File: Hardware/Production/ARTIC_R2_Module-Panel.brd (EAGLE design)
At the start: 154.2 x 147.3 mm, 2306 parts, among them J101 U.FL, J126 U.FL, J151 U.FL, J176 U.FL, J201 U.FL, J226 U.FL, J25 U.FL, J251 U.FL, J26 U.FL, J276 U.FL, J301 U.FL, J326 U.FL, J351 U.FL, J376 U.FL, J401 U.FL, J426 U.FL, J451 U.FL, J476 U.FL, J51 U.FL, J76 U.FL, K1 TLP3475R, K10 TLP3475R, K11 TLP3475R, K12 TLP3475R, K13 TLP3475R, K14 TLP3475R, K15 TLP3475R, K16 TLP3475R, K17 TLP3475R, K18 TLP3475R, K19 TLP3475R, K2 TLP3475R, K20 TLP3475R, K3 TLP3475R, K4 TLP3475R, K5 TLP3475R, K6 TLP3475R, K7 TLP3475R, K8 TLP3475R, K9 TLP3475R, Q1 5.8A/30V/35mΩ, Q10 5.8A/30V/35mΩ, Q11 5.8A/30V/35mΩ, Q12 5.8A/30V/35mΩ, Q13 5.8A/30V/35mΩ, Q14 5.8A/30V/35mΩ, Q15 5.8A/30V/35mΩ, Q16 5.8A/30V/35mΩ, Q17 5.8A/30V/35mΩ, Q18 5.8A/30V/35mΩ, Q19 5.8A/30V/35mΩ, Q2 5.8A/30V/35mΩ, Q20 5.8A/30V/35mΩ, Q3 5.8A/30V/35mΩ, Q4 5.8A/30V/35mΩ, Q5 5.8A/30V/35mΩ, Q6 5.8A/30V/35mΩ, Q7 5.8A/30V/35mΩ, Q8 5.8A/30V/35mΩ, Q9 5.8A/30V/35mΩ, U1 ADM4210-1, U10 1.8V/100mA, U100 1.8V/100mA, U101 3.0V, U102 ADM4210-1, U103 ARTIC_R2, U104 RFPA0133, U105 AS179-92LF, U106 1.8V/100mA, U107 3.0V, U108 ADM4210-1, U109 ARTIC_R2, U11 3.0V, U110 RFPA0133, U111 AS179-92LF, U112 1.8V/100mA, U113 3.0V, U114 ADM4210-1, U115 ARTIC_R2, U116 RFPA0133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

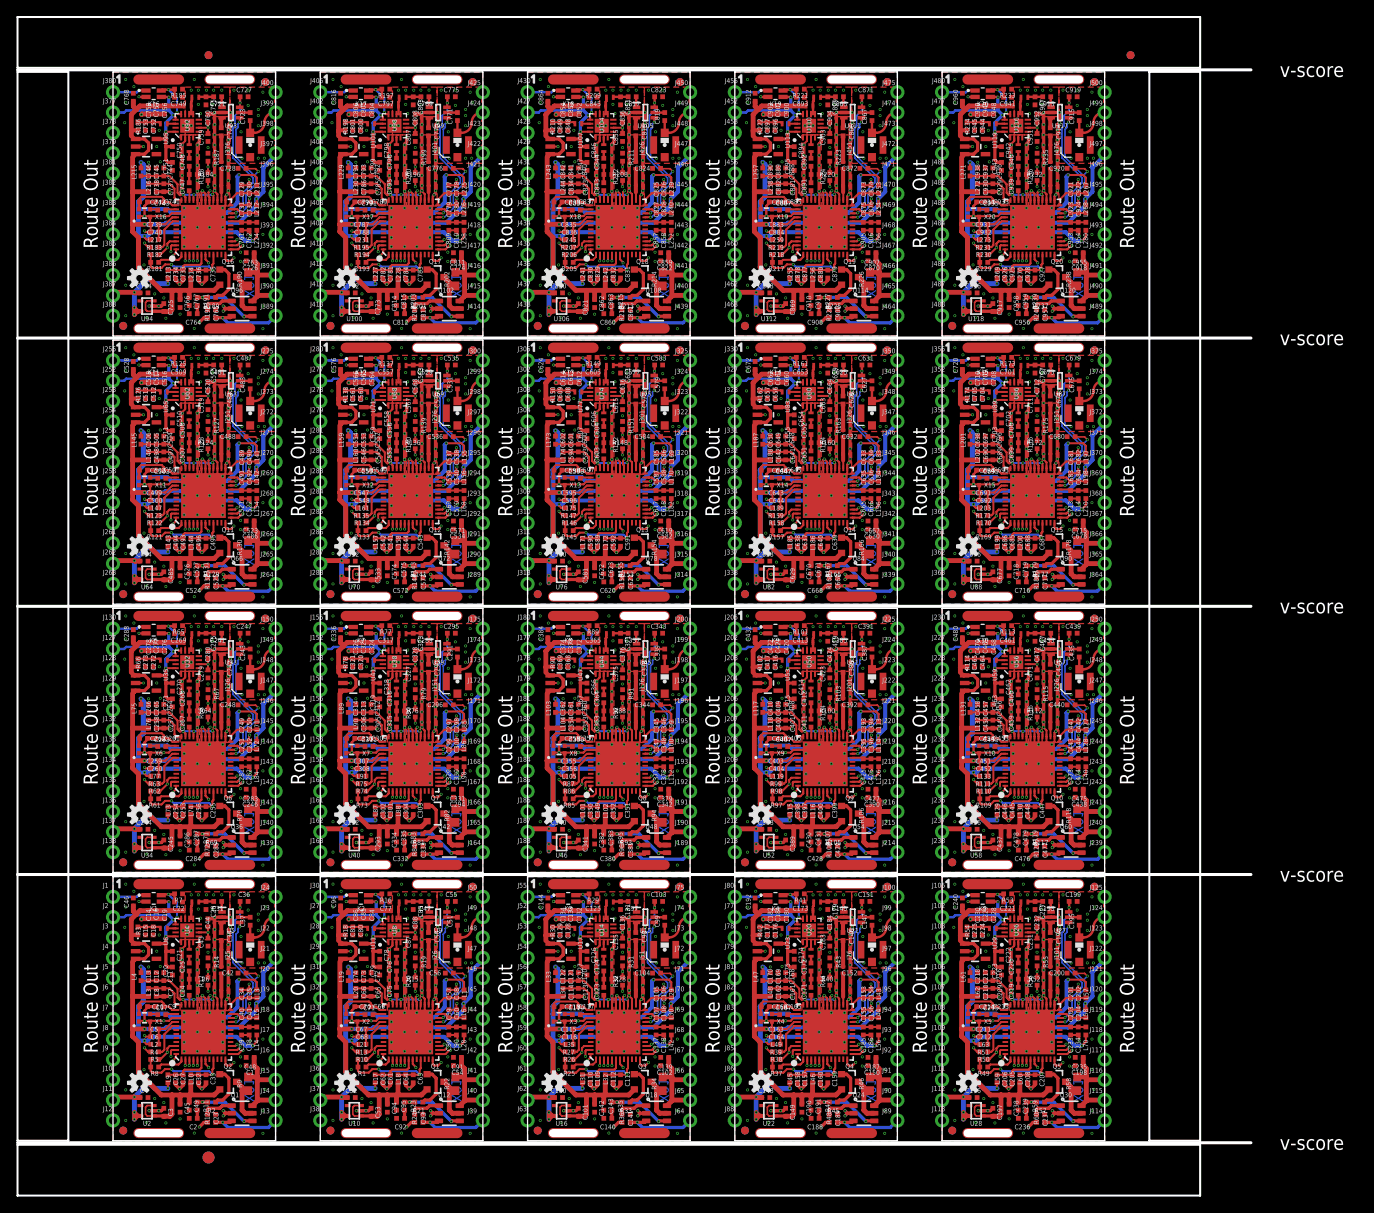
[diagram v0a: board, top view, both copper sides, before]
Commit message: Adding better castellated pads. Correcting cutouts for screen tabs.
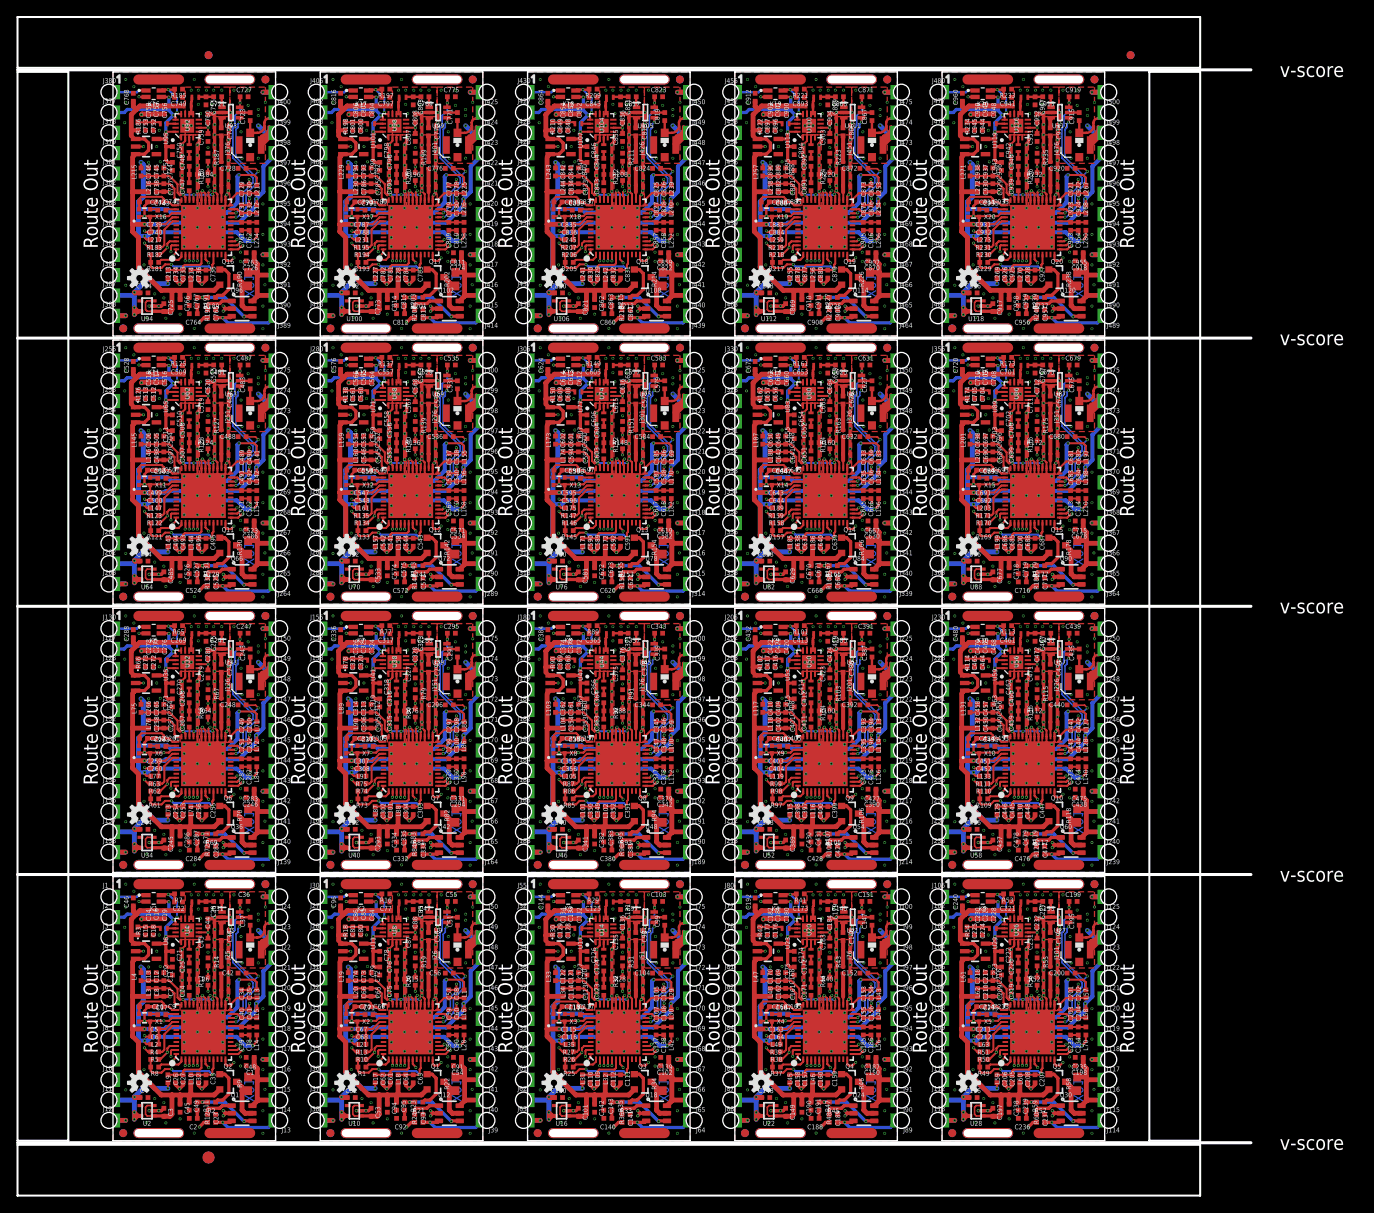
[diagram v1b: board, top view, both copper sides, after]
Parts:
- added LOGO21, LOGO22, LOGO23, LOGO24, LOGO25, LOGO26, LOGO27, LOGO28, LOGO29, LOGO30, LOGO31, LOGO32, LOGO33, LOGO34, LOGO35, LOGO36, LOGO37, LOGO38, LOGO39, LOGO40: OSHW-LOGOS, SparkFun-Aesthetics:OSHW-LOGO-S
- added SPARKX1, SPARKX10, SPARKX11, SPARKX12, SPARKX13, SPARKX14, SPARKX15, SPARKX16, SPARKX17, SPARKX18, SPARKX19, SPARKX2, SPARKX20, SPARKX3, SPARKX4, SPARKX5, SPARKX6, SPARKX7, SPARKX8, SPARKX9: SPARKX-LOGO4, SparkX:SPARKX-MEDIUM
- added U$100, U$126, U$152, U$178, U$204, U$22, U$230, U$256, U$282, U$308, U$334, U$360, U$386, U$412, U$438, U$464, U$48, U$490, U$516, U$74: (no value), output:#SCLK#0
- added U$101, U$127, U$153, U$179, U$205, U$23, U$231, U$257, U$283, U$309, U$335, U$361, U$387, U$413, U$439, U$465, U$49, U$491, U$517, U$75: (no value), output:#COPI#0
- added U$102, U$128, U$154, U$180, U$206, U$232, U$24, U$258, U$284, U$310, U$336, U$362, U$388, U$414, U$440, U$466, U$492, U$50, U$518, U$76: (no value), output:#CIPO#0
- added U$103, U$129, U$155, U$181, U$207, U$233, U$25, U$259, U$285, U$311, U$337, U$363, U$389, U$415, U$441, U$467, U$493, U$51, U$519, U$77: (no value), output:#1#8V_OUT#0
- added U$104, U$130, U$156, U$182, U$208, U$234, U$26, U$260, U$286, U$312, U$338, U$364, U$390, U$416, U$442, U$468, U$494, U$52, U$520, U$78: (no value), output:ARTIC_R20
- added U$105, U$131, U$157, U$183, U$209, U$235, U$261, U$27, U$287, U$313, U$339, U$365, U$391, U$417, U$443, U$469, U$495, U$53, U$79: (no value), output:10
- added U$106, U$107, U$108, U$109, U$132, U$133, U$134, U$135, U$158, U$159, U$160, U$161, U$184, U$185, U$186, U$187, U$210, U$211, U$212, U$213, U$236, U$237, U$238, U$239, U$262, U$263, U$264, U$265, U$28, U$288, U$289, U$29, U$290, U$291, U$30, U$31, U$314, U$315, U$316, U$317, U$340, U$341, U$342, U$343, U$366, U$367, U$368, U$369, U$392, U$393, U$394, U$395, U$418, U$419, U$420, U$421, U$444, U$445, U$446, U$447, U$470, U$471, U$472, U$473, U$496, U$497, U$498, U$499, U$54, U$55, U$56, U$57, U$80, U$81, U$82, U$83: (no value), output:#GND#0
- added U$110, U$136, U$162, U$188, U$214, U$240, U$266, U$292, U$318, U$32, U$344, U$370, U$396, U$422, U$448, U$474, U$500, U$58, U$84: (no value), output:#PWR_EN#0
- added U$111, U$112, U$137, U$138, U$163, U$164, U$189, U$190, U$215, U$216, U$241, U$242, U$267, U$268, U$293, U$294, U$319, U$320, U$33, U$34, U$345, U$346, U$371, U$372, U$397, U$398, U$423, U$424, U$449, U$450, U$475, U$476, U$501, U$502, U$59, U$60, U$85, U$86: (no value), output:#VIN#0
- added U$113, U$139, U$165, U$191, U$217, U$243, U$269, U$295, U$321, U$347, U$35, U$373, U$399, U$425, U$451, U$477, U$503, U$61, U$87: (no value), output:#FLSH_SCLK#0
- added U$114, U$140, U$166, U$192, U$218, U$244, U$270, U$296, U$322, U$348, U$36, U$374, U$400, U$426, U$452, U$478, U$504, U$62, U$88: (no value), output:#FLSH_SI#0
- added U$115, U$141, U$167, U$193, U$219, U$245, U$271, U$297, U$323, U$349, U$37, U$375, U$401, U$427, U$453, U$479, U$505, U$63, U$89: (no value), output:#FLSH_CEN#0
- added U$116, U$142, U$168, U$194, U$220, U$246, U$272, U$298, U$324, U$350, U$376, U$38, U$402, U$428, U$454, U$480, U$506, U$64, U$90: (no value), output:#FLSH_SO#0
- added U$117, U$143, U$169, U$195, U$221, U$247, U$273, U$299, U$325, U$351, U$377, U$39, U$403, U$429, U$455, U$481, U$507, U$65, U$91: (no value), output:#3#3V_OUT#0
- added U$118, U$144, U$170, U$196, U$222, U$248, U$274, U$300, U$326, U$352, U$378, U$40, U$404, U$430, U$456, U$482, U$508, U$66, U$92: (no value), output:#ANTENNA#0
- added U$119, U$145, U$171, U$197, U$223, U$249, U$275, U$301, U$327, U$353, U$379, U$405, U$41, U$431, U$457, U$483, U$509, U$67, U$93: (no value), output:#G8#0
- added U$120, U$146, U$172, U$198, U$224, U$250, U$276, U$302, U$328, U$354, U$380, U$406, U$42, U$432, U$458, U$484, U$510, U$68, U$94: (no value), output:#3#0V_OUT#0
- added U$121, U$147, U$173, U$199, U$225, U$251, U$277, U$303, U$329, U$355, U$381, U$407, U$43, U$433, U$459, U$485, U$511, U$69, U$95: (no value), output:#BOOT#0
- added U$122, U$148, U$174, U$200, U$226, U$252, U$278, U$304, U$330, U$356, U$382, U$408, U$434, U$44, U$460, U$486, U$512, U$70, U$96: (no value), output:#INT1#0
- added U$123, U$149, U$175, U$201, U$227, U$253, U$279, U$305, U$331, U$357, U$383, U$409, U$435, U$45, U$461, U$487, U$513, U$71, U$97: (no value), output:#INT2#0
- added U$124, U$150, U$176, U$202, U$228, U$254, U$280, U$306, U$332, U$358, U$384, U$410, U$436, U$46, U$462, U$488, U$514, U$72, U$98: (no value), output:#RESETB#0
- added U$125, U$151, U$177, U$203, U$21, U$229, U$255, U$281, U$307, U$333, U$359, U$385, U$411, U$437, U$463, U$47, U$489, U$515, U$73, U$99: (no value), output:#CS#0
- J1, J10, J100, J102, J103, J104, J105, J106, J107, J108, J109, J11, J110, J111, J112, J113, J114, J115, J116, J117, J118, J119, J12, J120, J121, J122, J123, J124, J125, J127, J128, J129, J13, J130, J131, J132, J133, J134, J135, J136, J137, J138, J139, J14, J140, J141, J142, J143, J144, J145, J146, J147, J148, J149, J15, J150, J152, J153, J154, J155, J156, J157, J158, J159, J16, J160, J161, J162, J163, J164, J165, J166, J167, J168, J169, J17, J170, J171, J172, J173, J174, J175, J177, J178, J179, J18, J180, J181, J182, J183, J184, J185, J186, J187, J188, J189, J19, J190, J191, J192, J193, J194, J195, J196, J197, J198, J199, J2, J20, J200, J202, J203, J204, J205, J206, J207, J208, J209, J21, J210, J211, J212, J213, J214, J215, J216, J217, J218, J219, J22, J220, J221, J222, J223, J224, J225, J227, J228, J229, J23, J230, J231, J232, J233, J234, J235, J236, J237, J238, J239, J24, J240, J241, J242, J243, J244, J245, J246, J247, J248, J249, J250, J252, J253, J254, J255, J256, J257, J258, J259, J260, J261, J262, J263, J264, J265, J266, J267, J268, J269, J27, J270, J271, J272, J273, J274, J275, J277, J278, J279, J28, J280, J281, J282, J283, J284, J285, J286, J287, J288, J289, J29, J290, J291, J292, J293, J294, J295, J296, J297, J298, J299, J3, J30, J300, J302, J303, J304, J305, J306, J307, J308, J309, J31, J310, J311, J312, J313, J314, J315, J316, J317, J318, J319, J32, J320, J321, J322, J323, J324, J325, J327, J328, J329, J33, J330, J331, J332, J333, J334, J335, J336, J337, J338, J339, J34, J340, J341, J342, J343, J344, J345, J346, J347, J348, J349, J35, J350, J352, J353, J354, J355, J356, J357, J358, J359, J36, J360, J361, J362, J363, J364, J365, J366, J367, J368, J369, J37, J370, J371, J372, J373, J374, J375, J377, J378, J379, J38, J380, J381, J382, J383, J384, J385, J386, J387, J388, J389, J39, J390, J391, J392, J393, J394, J395, J396, J397, J398, J399, J4, J40, J400, J402, J403, J404, J405, J406, J407, J408, J409, J41, J410, J411, J412, J413, J414, J415, J416, J417, J418, J419, J42, J420, J421, J422, J423, J424, J425, J427, J428, J429, J43, J430, J431, J432, J433, J434, J435, J436, J437, J438, J439, J44, J440, J441, J442, J443, J444, J445, J446, J447, J448, J449, J45, J450, J452, J453, J454, J455, J456, J457, J458, J459, J46, J460, J461, J462, J463, J464, J465, J466, J467, J468, J469, J47, J470, J471, J472, J473, J474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: device New_Parts_Connectors:1X01_CASTELLATED -> New_Parts_Connectors:CONN_01_CASTELLATED_4LAYER
- U$1, U$3, U$4, U$5: device output:10 -> output:#GND#0
- U$10: device output:10 -> output:#FLSH_SI#0
- U$11: device output:10 -> output:#FLSH_SO#0
- U$12: device output:10 -> output:#FLSH_CEN#0
- U$13: device output:10 -> output:#3#3V_OUT#0
- U$14: device output:10 -> output:#ANTENNA#0
- U$15: device output:10 -> output:#G8#0
- U$16: device output:10 -> output:#3#0V_OUT#0
- U$17: device output:10 -> output:#BOOT#0
- U$18: device output:10 -> output:#INT1#0
- U$19: device output:10 -> output:#INT2#0
- U$20: device output:10 -> output:#RESETB#0
- U$6: device output:10 -> output:#PWR_EN#0
- U$7, U$8: device output:10 -> output:#VIN#0
- U$9: device output:10 -> output:#FLSH_SCLK#0
- moved U$20 152.5 mm to (4.19, 17.8), flipped to the bottom
- moved U$19 135.3 mm to (3.17, 20.3), flipped to the bottom
- moved U$15 123.1 mm to (2.29, 30.5), flipped to the bottom
- moved U$18 120.5 mm to (3.05, 22.9), flipped to the bottom
- moved U$17 109.8 mm to (3.43, 25.4), flipped to the bottom
- moved U$5 105.7 mm to (2.92, 2.54), flipped to the bottom
- moved U$16 104.8 mm to (4.70, 27.9), flipped to the bottom
- moved U$10 101.5 mm to (16.3, 15.2), flipped to the bottom
- moved U$14 95.2 mm to (15.4, 27.9), flipped to the bottom
- moved U$13 84.7 mm to (15.7, 22.9), flipped to the bottom
- moved LOGO17 84.7 mm to (81.0, 40.8)
- moved U$11 82.8 mm to (16.0, 17.8), flipped to the bottom
- moved U$9 82.6 mm to (15.1, 12.7), flipped to the bottom
- moved U$12 79.7 mm to (15.4, 20.3), flipped to the bottom
- moved LOGO16 76.4 mm to (62.0, 58.9), flipped to the bottom, turned to 90 degrees
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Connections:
- net GND: now also SCREEN.1-1, SCREEN.1-16, SCREEN.2, SCREEN.3-1, SCREEN.3-16, SCREEN.4; no longer SCREEN.P$1, SCREEN.P$2, SCREEN.P$3, SCREEN.P$4
- net GND1: now also SCREEN1.1-1, SCREEN1.1-16, SCREEN1.2, SCREEN1.3-1, SCREEN1.3-16, SCREEN1.4; no longer SCREEN1.P$1, SCREEN1.P$2, SCREEN1.P$3, SCREEN1.P$4
- net GND10: now also SCREEN10.1-1, SCREEN10.1-16, SCREEN10.2, SCREEN10.3-1, SCREEN10.3-16, SCREEN10.4; no longer SCREEN10.P$1, SCREEN10.P$2, SCREEN10.P$3, SCREEN10.P$4
- net GND11: now also SCREEN11.1-1, SCREEN11.1-16, SCREEN11.2, SCREEN11.3-1, SCREEN11.3-16, SCREEN11.4; no longer SCREEN11.P$1, SCREEN11.P$2, SCREEN11.P$3, SCREEN11.P$4
- net GND12: now also SCREEN12.1-1, SCREEN12.1-16, SCREEN12.2, SCREEN12.3-1, SCREEN12.3-16, SCREEN12.4; no longer SCREEN12.P$1, SCREEN12.P$2, SCREEN12.P$3, SCREEN12.P$4
- net GND13: now also SCREEN13.1-1, SCREEN13.1-16, SCREEN13.2, SCREEN13.3-1, SCREEN13.3-16, SCREEN13.4; no longer SCREEN13.P$1, SCREEN13.P$2, SCREEN13.P$3, SCREEN13.P$4
- net GND14: now also SCREEN14.1-1, SCREEN14.1-16, SCREEN14.2, SCREEN14.3-1, SCREEN14.3-16, SCREEN14.4; no longer SCREEN14.P$1, SCREEN14.P$2, SCREEN14.P$3, SCREEN14.P$4
- net GND15: now also SCREEN15.1-1, SCREEN15.1-16, SCREEN15.2, SCREEN15.3-1, SCREEN15.3-16, SCREEN15.4; no longer SCREEN15.P$1, SCREEN15.P$2, SCREEN15.P$3, SCREEN15.P$4
- net GND16: now also SCREEN16.1-1, SCREEN16.1-16, SCREEN16.2, SCREEN16.3-1, SCREEN16.3-16, SCREEN16.4; no longer SCREEN16.P$1, SCREEN16.P$2, SCREEN16.P$3, SCREEN16.P$4
- net GND17: now also SCREEN17.1-1, SCREEN17.1-16, SCREEN17.2, SCREEN17.3-1, SCREEN17.3-16, SCREEN17.4; no longer SCREEN17.P$1, SCREEN17.P$2, SCREEN17.P$3, SCREEN17.P$4
- net GND18: now also SCREEN18.1-1, SCREEN18.1-16, SCREEN18.2, SCREEN18.3-1, SCREEN18.3-16, SCREEN18.4; no longer SCREEN18.P$1, SCREEN18.P$2, SCREEN18.P$3, SCREEN18.P$4
- net GND19: now also SCREEN19.1-1, SCREEN19.1-16, SCREEN19.2, SCREEN19.3-1, SCREEN19.3-16, SCREEN19.4; no longer SCREEN19.P$1, SCREEN19.P$2, SCREEN19.P$3, SCREEN19.P$4
- net GND2: now also SCREEN2.1-1, SCREEN2.1-16, SCREEN2.2, SCREEN2.3-1, SCREEN2.3-16, SCREEN2.4; no longer SCREEN2.P$1, SCREEN2.P$2, SCREEN2.P$3, SCREEN2.P$4
- net GND3: now also SCREEN3.1-1, SCREEN3.1-16, SCREEN3.2, SCREEN3.3-1, SCREEN3.3-16, SCREEN3.4; no longer SCREEN3.P$1, SCREEN3.P$2, SCREEN3.P$3, SCREEN3.P$4
- net GND4: now also SCREEN4.1-1, SCREEN4.1-16, SCREEN4.2, SCREEN4.3-1, SCREEN4.3-16, SCREEN4.4; no longer SCREEN4.P$1, SCREEN4.P$2, SCREEN4.P$3, SCREEN4.P$4
- net GND5: now also SCREEN5.1-1, SCREEN5.1-16, SCREEN5.2, SCREEN5.3-1, SCREEN5.3-16, SCREEN5.4; no longer SCREEN5.P$1, SCREEN5.P$2, SCREEN5.P$3, SCREEN5.P$4
- net GND6: now also SCREEN6.1-1, SCREEN6.1-16, SCREEN6.2, SCREEN6.3-1, SCREEN6.3-16, SCREEN6.4; no longer SCREEN6.P$1, SCREEN6.P$2, SCREEN6.P$3, SCREEN6.P$4
- net GND7: now also SCREEN7.1-1, SCREEN7.1-16, SCREEN7.2, SCREEN7.3-1, SCREEN7.3-16, SCREEN7.4; no longer SCREEN7.P$1, SCREEN7.P$2, SCREEN7.P$3, SCREEN7.P$4
- net GND8: now also SCREEN8.1-1, SCREEN8.1-16, SCREEN8.2, SCREEN8.3-1, SCREEN8.3-16, SCREEN8.4; no longer SCREEN8.P$1, SCREEN8.P$2, SCREEN8.P$3, SCREEN8.P$4
- net GND9: now also SCREEN9.1-1, SCREEN9.1-16, SCREEN9.2, SCREEN9.3-1, SCREEN9.3-16, SCREEN9.4; no longer SCREEN9.P$1, SCREEN9.P$2, SCREEN9.P$3, SCREEN9.P$4
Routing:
- net GND6: track 84.7 -> 117.5 mm
- net GND15: track 84.7 -> 117.5 mm
- net GND11: track 84.7 -> 117.5 mm
- net GND5: track 84.7 -> 117.5 mm
- net GND10: track 84.7 -> 117.5 mm
- net GND16: track 84.7 -> 117.5 mm
- net GND1: track 84.7 -> 117.5 mm
- net GND: track 84.7 -> 117.5 mm
- net GND17: track 84.7 -> 117.5 mm
- net GND7: track 84.7 -> 117.5 mm
- net GND19: track 84.7 -> 117.5 mm
- net GND12: track 84.7 -> 117.5 mm
- net GND18: track 84.7 -> 117.5 mm
- net GND2: track 84.7 -> 117.5 mm
- net GND14: track 84.7 -> 117.5 mm
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
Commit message: Updated the screening can
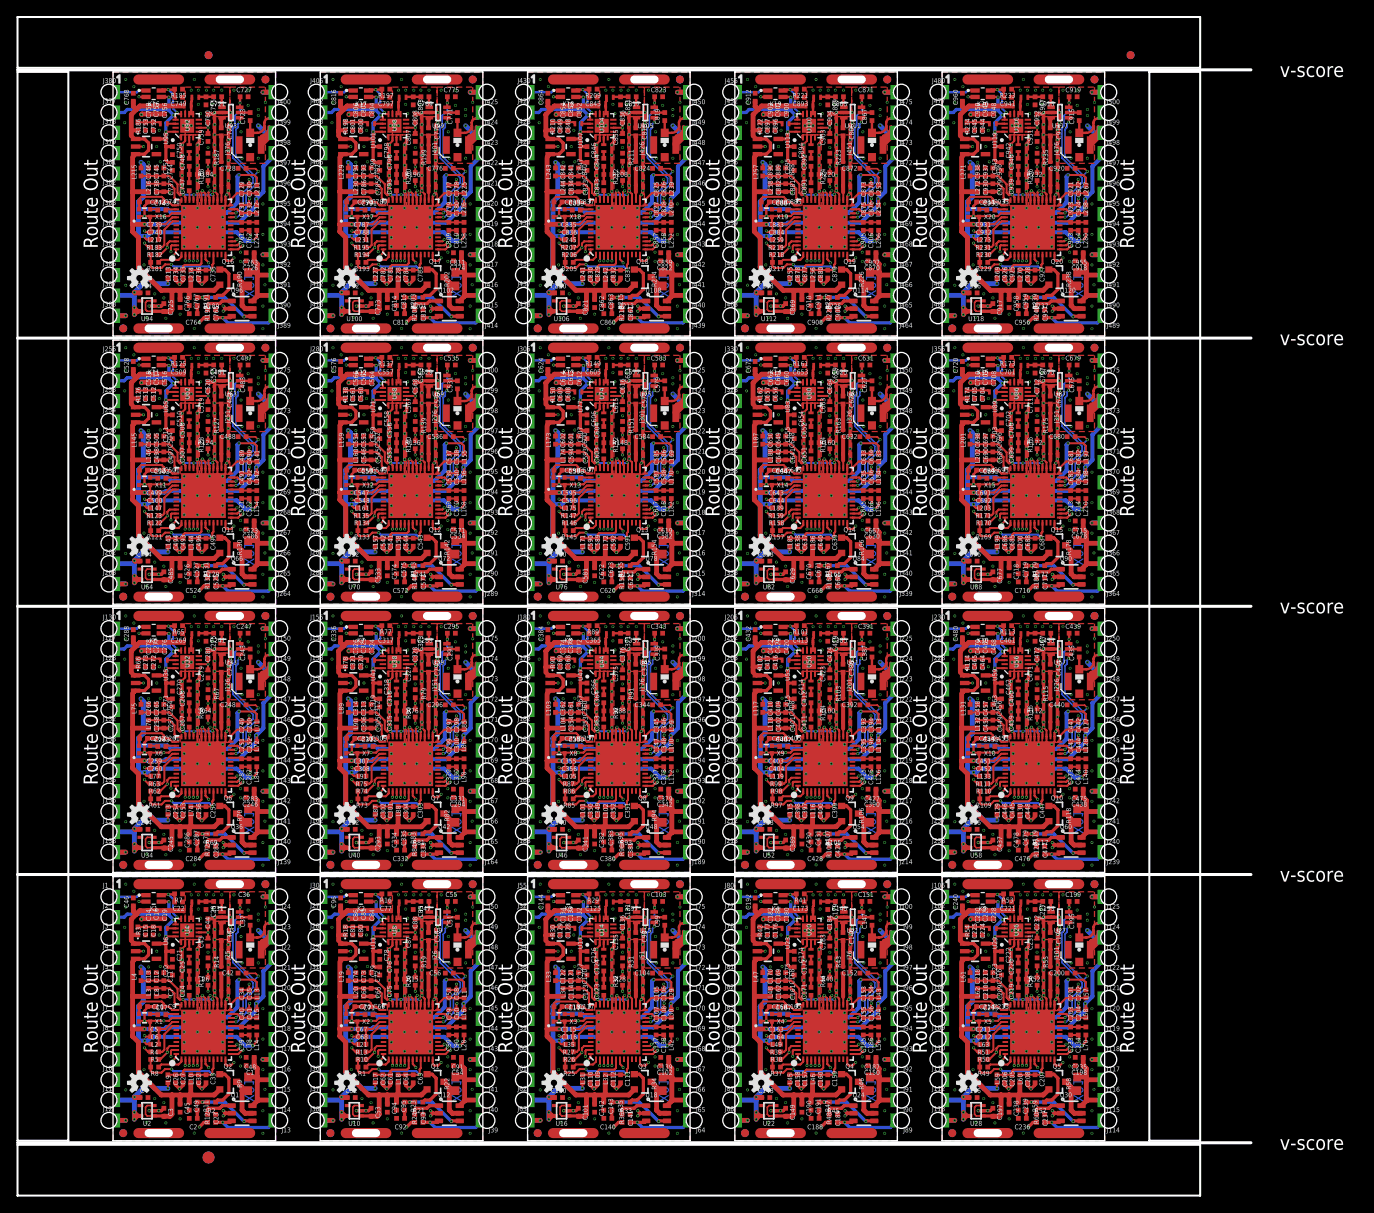
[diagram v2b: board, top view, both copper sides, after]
